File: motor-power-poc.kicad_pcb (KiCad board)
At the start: 4 copper layers, 70 x 50 mm, 160 parts, among them J1 Conn_01x04_Pin, J2 USB_C_Receptacle_USB2.0_14P, J3 Conn_01x02, J4 Conn_02x02_Counter_Clockwise, J5 Conn_02x06_Counter_Clockwise, M1 Motor_Servo, M2 Motor_Servo, M3 DC, Q1 Q_NMOS, Q10 Q_NMOS, Q2 Q_NMOS, Q3 Q_NMOS, Q4 Q_NMOS, Q5 Q_NMOS, Q6 Q_NMOS, Q7 Q_NMOS, Q8 Q_NMOS, Q9 Q_NMOS, SW1 SW_Push, SW2 SW_Push, U1 QRE1113GR, U10 CJ431, U11 DRV8701, U2 QRE1113GR, U3 QRE1113GR, U4 ESP32-S3FH4R2, U5 LM74502, U6 TPS5430DDA, U7 TPS56A37, U8 TPS2121, U9 LDL212PV33R, Y1 48M

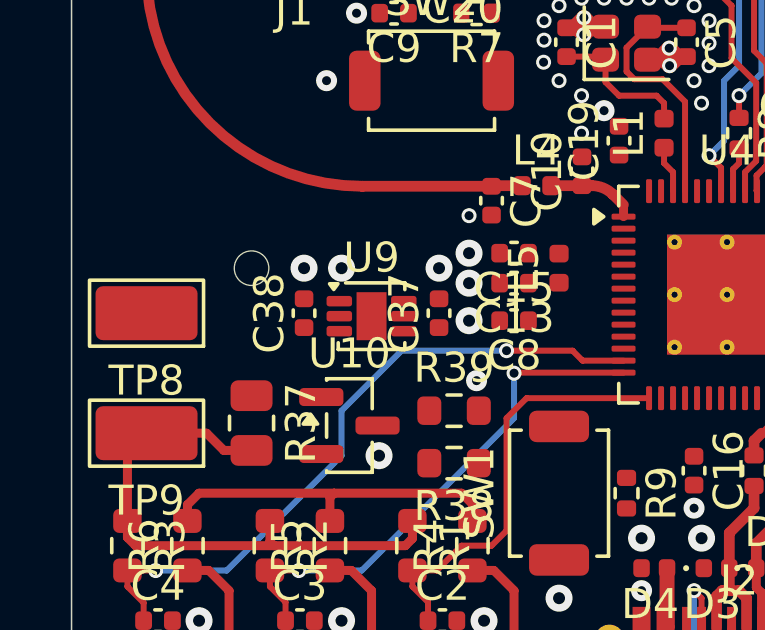
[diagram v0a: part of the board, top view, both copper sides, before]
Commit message: pcb: add 3v3 ldo routing
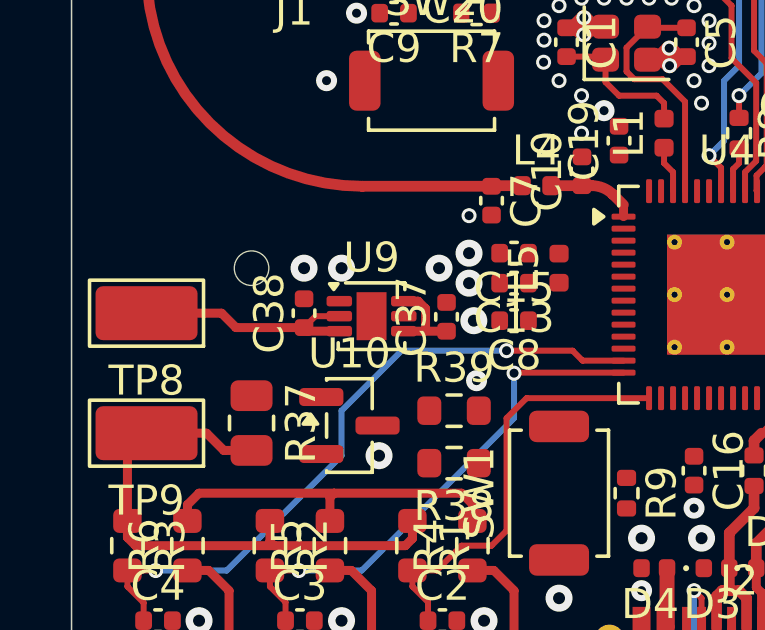
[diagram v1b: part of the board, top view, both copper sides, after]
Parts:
- moved C37 0.28 mm to (124.5, 85.6)
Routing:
- net +3V3: track 11.9 -> 19.9 mm
- net +5V: track 0.00 -> 2.75 mm
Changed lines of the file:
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@@
 	(footprint "Capacitor_SMD:C_0402_1005Metric"
 		(layer "F.Cu")
-		(at 124.25 85.5 90)
+		(at 124.5 85.62143 90)
 		(descr "Capacitor SMD 0402 (1005 Metric), square (rectangular) end terminal, IPC-7351 nominal, (Body size source: IPC-SM-782 page 76, https://www.pcb-3d.com/wordpress/wp-content/uploads/ipc-sm-782a_amendment_1_and_2.pdf), generated with kicad-footprint-generator")
 		(tags "capacitor")
@@
 	)
 	(segment
+		(start 120.925 86.1)
+		(end 119.87 86.1)
+		(width 0.3)
+		(layer "F.Cu")
+		(net 9)
+	)
+	(segment
+		(start 119.87 86.1)
+		(end 119.75 85.98)
+		(width 0.3)
+		(layer "F.Cu")
+		(net 9)
+	)
+	(segment
+		(start 120.925 85.6)
+		(end 120.13 85.6)
+		(width 0.2)
+		(layer "F.Cu")
+		(net 9)
+	)
+	(segment
 		(start 125.3625 91.8625)
 		(end 125.3625 92.425)
@@
 	)
 	(segment
+		(start 119.75 85.98)
+		(end 117.48 85.98)
+		(width 0.3)
+		(layer "F.Cu")
+		(net 9)
+	)
+	(segment
 		(start 120.6125 92.425)
 		(end 120.6125 91.6375)
@@
 	)
 	(segment
+		(start 120.13 85.6)
+		(end 119.75 85.98)
+		(width 0.2)
+		(layer "F.Cu")
+		(net 9)
+	)
+	(segment
+		(start 117.48 85.98)
+		(end 117 85.5)
+		(width 0.3)
+		(layer "F.Cu")
+		(net 9)
+	)
+	(segment
+		(start 117 85.5)
+		(end 114.5 85.5)
+		(width 0.3)
+		(layer "F.Cu")
+		(net 9)
+	)
+	(segment
 		(start 115.8625 92.425)
 		(end 115.8625 91.8875)
@@
 	)
 	(segment
+		(start 124.220766 86.10143)
+		(end 123.75 86.10143)
+		(width 0.3)
+		(layer "F.Cu")
+		(net 14)
+	)
+	(segment
+		(start 123.551848 85.1)
+		(end 123.075 85.1)
+		(width 0.3)
+		(layer "F.Cu")
+		(net 14)
+	)
+	(segment
+		(start 123.801 86.05043)
+		(end 123.801 85.349152)
+		(width 0.3)
+		(layer "F.Cu")
+		(net 14)
+	)
+	(segment
+		(start 123.801 85.349152)
+		(end 123.551848 85.1)
+		(width 0.3)
+		(layer "F.Cu")
+		(net 14)
+	)
+	(segment
+		(start 123.75 86.10143)
+		(end 123.801 86.05043)
+		(width 0.3)
+		(layer "F.Cu")
+		(net 14)
+	)
+	(segment
+		(start 123.75 86.10143)
+		(end 123.07643 86.10143)
+		(width 0.3)
+		(layer "F.Cu")
+		(net 14)
+	)
+	(segment
+		(start 123.07643 86.10143)
+		(end 123.075 86.1)
+		(width 0.3)
+		(layer "F.Cu")
+		(net 14)
+	)
+	(segment
 		(start 168.9 87.6)
 		(end 169 87.5)
@@
 	)
 	(via
-		(at 125.25 85.75)
+		(at 125.409159 85.750326)
 		(size 0.9)
 		(drill 0.4)

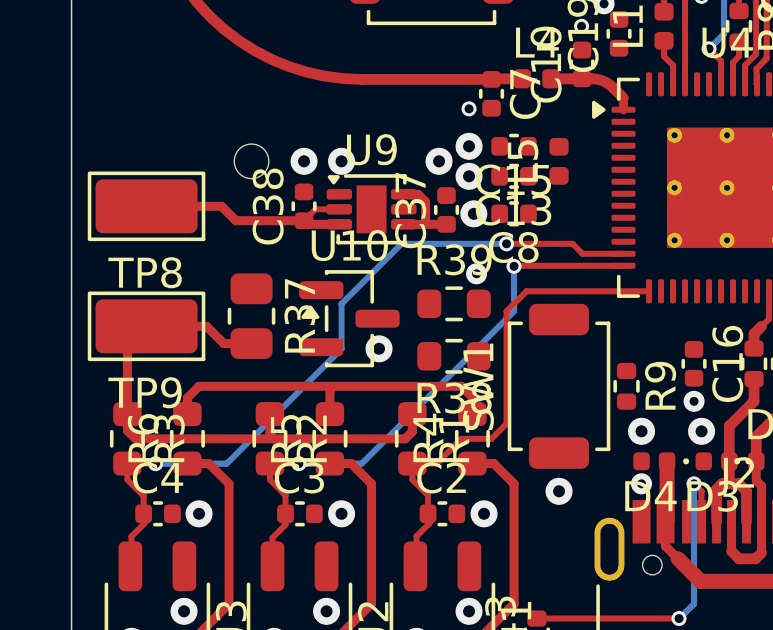
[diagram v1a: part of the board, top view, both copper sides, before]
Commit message: pcb: add 3v reference routing
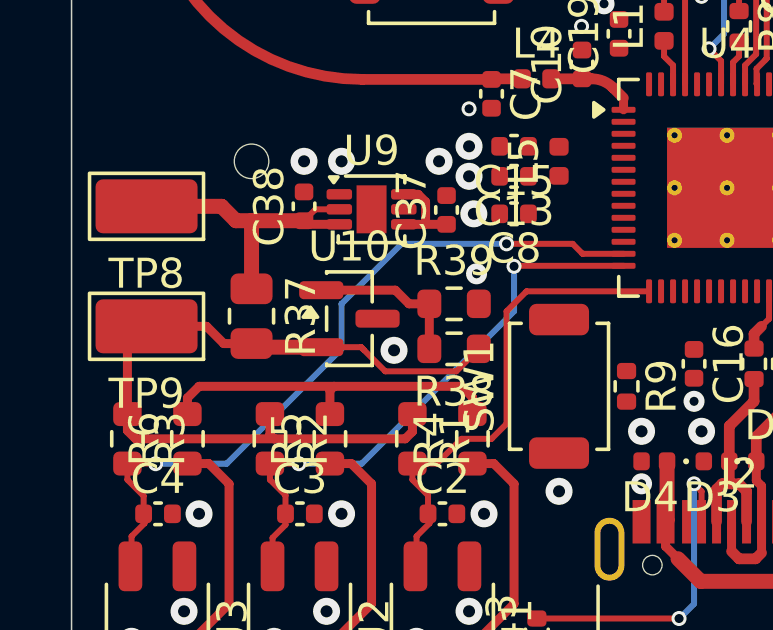
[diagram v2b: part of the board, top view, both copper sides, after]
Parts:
- moved R38 0.25 mm to (124.8, 90.2)
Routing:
- net +3V: track 18.7 -> 27.0 mm
- net Net-(U10-REF): track 0.00 -> 5.54 mm
- net +3V3: track 19.9 -> 22.2 mm
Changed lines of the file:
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@@
 	(footprint "Resistor_SMD:R_0603_1608Metric"
 		(layer "F.Cu")
-		(at 124.75 90.5 180)
+		(at 124.75 90.25 180)
 		(descr "Resistor SMD 0603 (1608 Metric), square (rectangular) end terminal, IPC-7351 nominal, (Body size source: IPC-SM-782 page 72, https://www.pcb-3d.com/wordpress/wp-content/uploads/ipc-sm-782a_amendment_1_and_2.pdf), generated with kicad-footprint-generator")
 		(tags "resistor")
@@
 	)
 	(segment
+		(start 119.75 85.98)
+		(end 118 85.98)
+		(width 0.5)
+		(layer "F.Cu")
+		(net 9)
+	)
+	(segment
 		(start 120.925 85.6)
 		(end 120.13 85.6)
@@
 	)
 	(segment
-		(start 119.75 85.98)
+		(start 118 85.98)
 		(end 117.48 85.98)
-		(width 0.3)
+		(width 0.5)
 		(layer "F.Cu")
 		(net 9)
@@
 	)
 	(segment
+		(start 118 88.25)
+		(end 118 85.98)
+		(width 0.5)
+		(layer "F.Cu")
+		(net 9)
+	)
+	(segment
 		(start 120.13 85.6)
 		(end 119.75 85.98)
@@
 		(start 117.48 85.98)
 		(end 117 85.5)
-		(width 0.3)
+		(width 0.5)
 		(layer "F.Cu")
 		(net 9)
@@
 		(start 117 85.5)
 		(end 114.5 85.5)
-		(width 0.3)
+		(width 0.5)
 		(layer "F.Cu")
 		(net 9)
@@
 	)
 	(segment
+		(start 121.729318 90.270682)
+		(end 121.653179 90.194543)
+		(width 0.2)
+		(layer "F.Cu")
+		(net 54)
+	)
+	(segment
+		(start 121.653636 90.195)
+		(end 120.325 90.195)
+		(width 0.2)
+		(layer "F.Cu")
+		(net 54)
+	)
+	(segment
 		(start 114.1375 93.25)
 		(end 113.8625 92.975)
@@
 	)
 	(segment
+		(start 124.825 91)
+		(end 122.458636 91)
+		(width 0.2)
+		(layer "F.Cu")
+		(net 54)
+	)
+	(segment
 		(start 123.124 93.25)
 		(end 118.75 93.25)
@@
 	)
 	(segment
+		(start 122.458636 91)
+		(end 121.729318 90.270682)
+		(width 0.2)
+		(layer "F.Cu")
+		(net 54)
+	)
+	(segment
 		(start 113.8625 92.425)
 		(end 113.8625 90.1375)
@@
 	)
 	(segment
+		(start 120.325 90.195)
+		(end 118.12 90.195)
+		(width 0.5)
+		(layer "F.Cu")
+		(net 54)
+	)
+	(segment
+		(start 121.729318 90.270682)
+		(end 121.653636 90.195)
+		(width 0.2)
+		(layer "F.Cu")
+		(net 54)
+	)
+	(segment
 		(start 123.3625 92.425)
 		(end 123.3625 93.0115)
@@
 	)
 	(segment
+		(start 118.12 90.195)
+		(end 118 90.075)
+		(width 0.5)
+		(layer "F.Cu")
+		(net 54)
+	)
+	(segment
 		(start 123.3625 93.0115)
 		(end 123.124 93.25)
@@
 	)
 	(segment
+		(start 125.575 90.25)
+		(end 124.825 91)
+		(width 0.2)
+		(layer "F.Cu")
+		(net 54)
+	)
+	(segment
 		(start 118.6125 93.1125)
 		(end 118.75 93.25)
@@
 	)
 	(segment
+		(start 123.925 90.5)
+		(end 123.925 88.75)
+		(width 0.3)
+		(layer "F.Cu")
+		(net 70)
+	)
+	(segment
+		(start 123.925 88.75)
+		(end 123.25 88.75)
+		(width 0.3)
+		(layer "F.Cu")
+		(net 70)
+	)
+	(segment
+		(start 122.795 88.295)
+		(end 120.325 88.295)
+		(width 0.3)
+		(layer "F.Cu")
+		(net 70)
+	)
+	(segment
+		(start 123.25 88.75)
+		(end 122.795 88.295)
+		(width 0.3)
+		(layer "F.Cu")
+		(net 70)
+	)
+	(segment
 		(start 179 87.1445)
 		(end 179 85.25)
@@
 	)
 	(via
-		(at 122.25 90.25)
+		(at 122.75 90.3)
 		(size 0.9)
 		(drill 0.4)

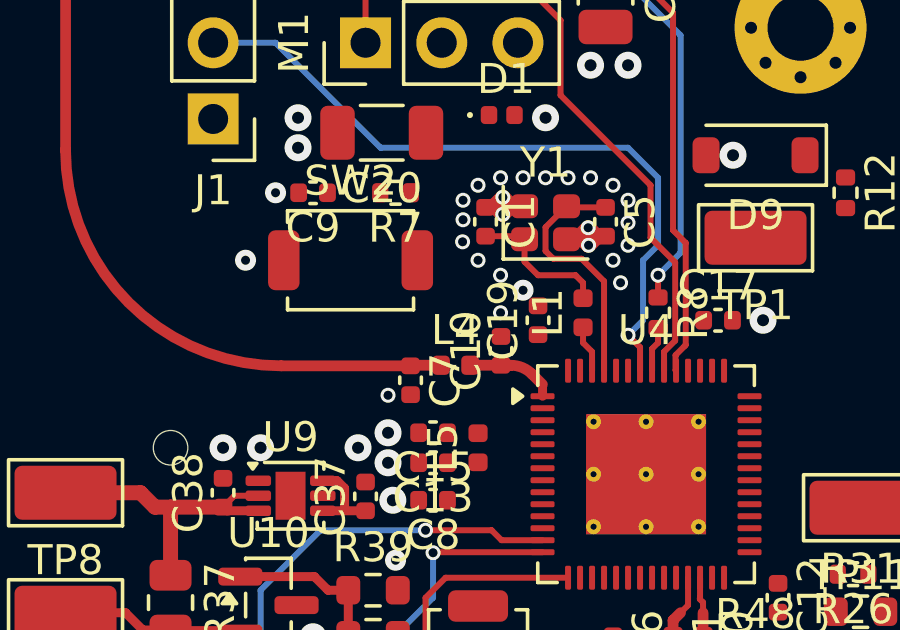
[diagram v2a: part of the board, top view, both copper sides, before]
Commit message: pcb: add CHIP_PU routing
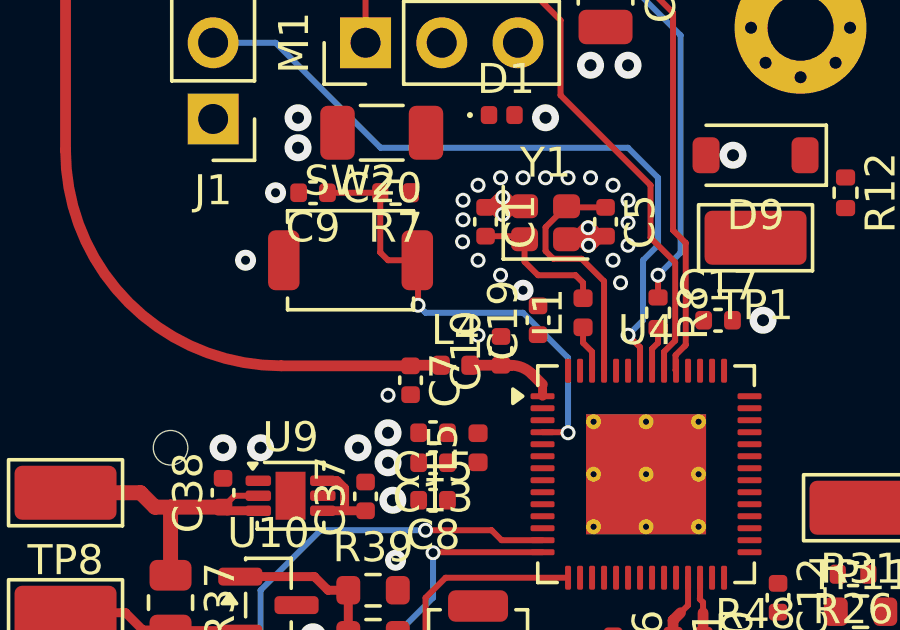
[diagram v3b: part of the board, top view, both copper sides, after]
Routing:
- net /CHIP_PU: track 0.00 -> 15.7 mm, vias 0 -> 2
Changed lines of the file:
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@@
+	)
+	(segment
+		(start 126.225 77.75)
+		(end 125.25 77.75)
+		(width 0.2)
+		(layer "F.Cu")
+		(net 10)
+	)
+	(segment
+		(start 131.2325 83.4825)
+		(end 131.25 83.5)
+		(width 0.2)
+		(layer "F.Cu")
+		(net 10)
+	)
+	(segment
+		(start 125.25 77.75)
+		(end 124.99 77.49)
+		(width 0.2)
+		(layer "F.Cu")
+		(net 10)
+	)
+	(segment
+		(start 126.25 79.25)
+		(end 126.25 77.775)
+		(width 0.2)
+		(layer "F.Cu")
+		(net 10)
+	)
+	(segment
+		(start 123.23 75.5)
+		(end 124.99 75.5)
+		(width 0.2)
+		(layer "F.Cu")
+		(net 10)
+	)
+	(segment
+		(start 126.25 77.775)
+		(end 126.225 77.75)
+		(width 0.2)
+		(layer "F.Cu")
+		(net 10)
+	)
+	(segment
+		(start 130.4 83.4825)
+		(end 131.2325 83.4825)
+		(width 0.2)
+		(layer "F.Cu")
+		(net 10)
+	)
+	(segment
+		(start 124.99 77.49)
+		(end 124.99 75.5)
+		(width 0.2)
+		(layer "F.Cu")
+		(net 10)
+	)
+	(via
+		(at 126.25 79.25)
+		(size 0.5)
+		(drill 0.3)
+		(layers "F.Cu" "B.Cu")
+		(net 10)
+	)
+	(via
+		(at 131.25 83.5)
+		(size 0.5)
+		(drill 0.3)
+		(layers "F.Cu" "B.Cu")
+		(net 10)
+	)
+	(segment
+		(start 129.75 79.5)
+		(end 126.5 79.5)
+		(width 0.2)
+		(layer "B.Cu")
+		(net 10)
+	)
+	(segment
+		(start 126.5 79.5)
+		(end 126.25 79.25)
+		(width 0.2)
+		(layer "B.Cu")
+		(net 10)
+	)
+	(segment
+		(start 131.25 83.5)
+		(end 131.25 81)
+		(width 0.2)
+		(layer "B.Cu")
+		(net 10)
+	)
+	(segment
+		(start 131.25 81)
+		(end 129.75 79.5)
+		(width 0.2)
+		(layer "B.Cu")
+		(net 10)
 	)
 	(segment
@@
 	)
 	(via
-		(at 129 79.5)
-		(size 0.5)
-		(drill 0.3)
+		(at 128.25 80.25)
+		(size 0.5)
+		(drill 0.3)

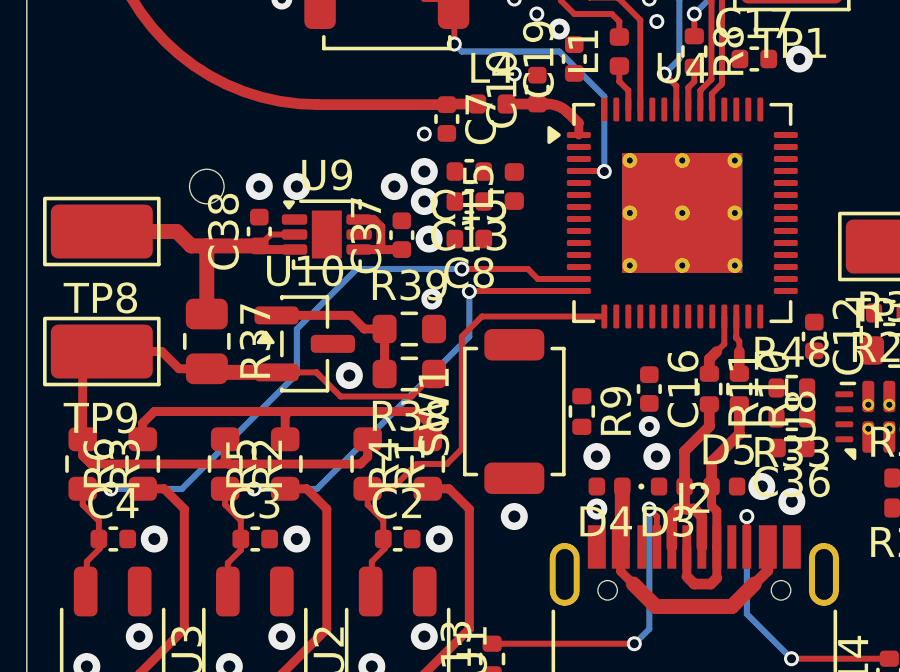
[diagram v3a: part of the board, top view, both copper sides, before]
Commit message: pcb: add BOOT routing
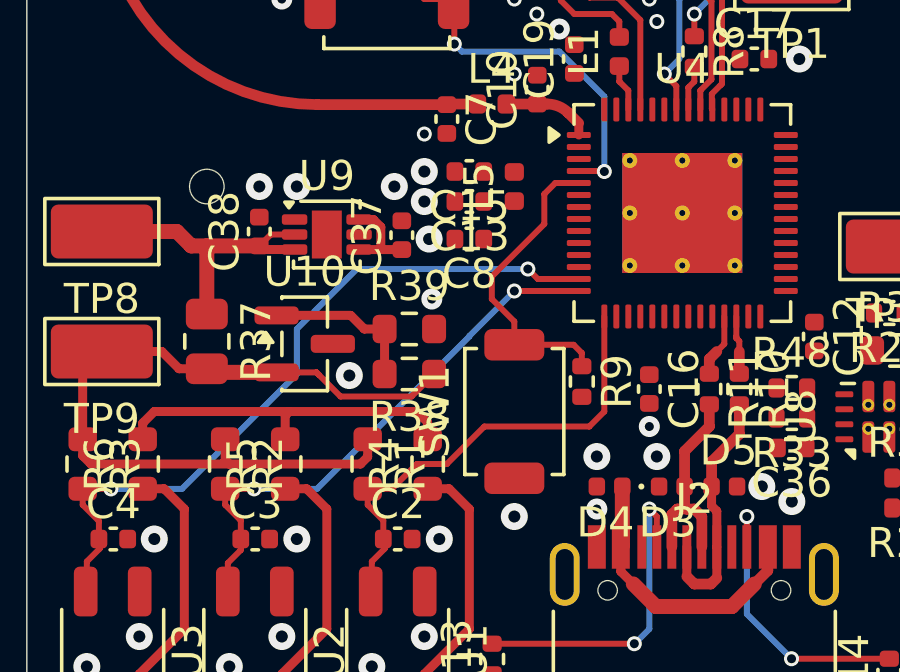
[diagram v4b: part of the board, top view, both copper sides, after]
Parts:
- moved R9 1.00 mm to (130.5, 90.5)
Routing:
- net /BOOT: track 0.00 -> 10.2 mm
- net /LS2: track 19.2 -> 18.4 mm
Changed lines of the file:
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@@
 	(footprint "Resistor_SMD:R_0402_1005Metric"
 		(layer "F.Cu")
-		(at 130.5 91.5 -90)
+		(at 130.5 90.5 -90)
 		(descr "Resistor SMD 0402 (1005 Metric), square (rectangular) end terminal, IPC-7351 nominal, (Body size source: IPC-SM-782 page 72, https://www.pcb-3d.com/wordpress/wp-content/uploads/ipc-sm-782a_amendment_1_and_2.pdf), generated with kicad-footprint-generator")
 		(tags "resistor")
@@
 	)
 	(segment
+		(start 127.25 92)
+		(end 130.75 92)
+		(width 0.2)
+		(layer "F.Cu")
+		(net 3)
+	)
+	(segment
 		(start 123.8825 95.1325)
 		(end 123.3625 94.6125)
@@
 	)
 	(segment
-		(start 127.1675 88.3325)
-		(end 131.25 88.3325)
+		(start 125 93.25)
+		(end 126 93.25)
 		(width 0.2)
 		(layer "F.Cu")
@@
 	)
 	(segment
-		(start 126.5 92.75)
-		(end 126.5 89)
+		(start 130.75 92)
+		(end 131.25 91.5)
 		(width 0.2)
 		(layer "F.Cu")
@@
 	)
 	(segment
-		(start 123.3625 94.075)
-		(end 124.175 94.075)
+		(start 131.25 91.5)
+		(end 131.25 88.3325)
 		(width 0.2)
 		(layer "F.Cu")
@@
 	)
 	(segment
-		(start 125 93.25)
-		(end 126 93.25)
+		(start 126 93.25)
+		(end 127.25 92)
+		(width 0.2)
+		(layer "F.Cu")
+		(net 3)
+	)
+	(segment
+		(start 123.3625 94.075)
+		(end 124.175 94.075)
 		(width 0.2)
 		(layer "F.Cu")
@@
 	)
 	(segment
-		(start 126.5 89)
-		(end 127.1675 88.3325)
-		(width 0.2)
-		(layer "F.Cu")
-		(net 3)
-	)
-	(segment
-		(start 126 93.25)
-		(end 126.5 92.75)
-		(width 0.2)
-		(layer "F.Cu")
-		(net 3)
-	)
-	(segment
 		(start 118.7 96.55)
 		(end 119.1325 96.1175)
@@
 	)
 	(segment
-		(start 126.7675 87.4825)
-		(end 126.75 87.5)
-		(width 0.2)
-		(layer "F.Cu")
-		(net 4)
-	)
-	(segment
 		(start 119.1325 95.1325)
 		(end 118.6125 94.6125)
@@
 	)
 	(segment
-		(start 130.4 87.4825)
-		(end 126.7675 87.4825)
+		(start 128.25 87.4825)
+		(end 130.4 87.4825)
 		(width 0.2)
 		(layer "F.Cu")
@@
 	)
 	(via
-		(at 126.75 87.5)
+		(at 128.25 87.4825)
 		(size 0.5)
 		(drill 0.3)
@@
 	)
 	(segment
-		(start 119.576653 94.07944)
+		(start 126.75 89)
 		(end 121.67056 94.07944)
 		(width 0.2)
@@
 	)
 	(segment
-		(start 126.75 89)
-		(end 126.75 87.5)
+		(start 126.75 88.9825)
+		(end 126.75 89)
 		(width 0.2)
 		(layer "B.Cu")
@@
 	(segment
 		(start 121.67056 94.07944)
-		(end 126.75 89)
+		(end 119.576653 94.07944)
+		(width 0.2)
+		(layer "B.Cu")
+		(net 4)
+	)
+	(segment
+		(start 128.25 87.4825)
+		(end 126.75 88.9825)
 		(width 0.2)
 		(layer "B.Cu")
@@
 	)
 	(segment
+		(start 129.034166 87.0825)
+		(end 130.4 87.0825)
+		(width 0.2)
+		(layer "F.Cu")
+		(net 5)
+	)
+	(segment
 		(start 114 97.45)
 		(end 114 96.5)
@@
 	)
 	(segment
-		(start 129.034166 87.0825)
-		(end 130.4 87.0825)
-		(width 0.2)
-		(layer "F.Cu")
-		(net 5)
-	)
-	(segment
-		(start 126.5 86.75)
-		(end 128.701666 86.75)
-		(width 0.2)
-		(layer "F.Cu")
-		(net 5)
-	)
-	(segment
 		(start 114.4325 96.0675)
 		(end 114.4325 95.7)
@@
 	)
 	(via
-		(at 126.5 86.75)
+		(at 128.701666 86.75)
 		(size 0.5)
 		(drill 0.3)
@@
 	)
 	(segment
-		(start 117.17056 94.07944)
-		(end 114.803296 94.07944)
+		(start 128.701666 86.75)
+		(end 123 86.75)
 		(width 0.2)
 		(layer "B.Cu")
@@
 	)
 	(segment
-		(start 126.5 86.75)
-		(end 123 86.75)
+		(start 123 86.75)
+		(end 121 88.75)
 		(width 0.2)
 		(layer "B.Cu")
@@
 	)
 	(segment
-		(start 123 86.75)
-		(end 121 88.75)
+		(start 117.17056 94.07944)
+		(end 114.803296 94.07944)
 		(width 0.2)
 		(layer "B.Cu")
@@
 	)
 	(segment
+		(start 130.5 89.55)
+		(end 130.225 89.275)
+		(width 0.2)
+		(layer "F.Cu")
+		(net 59)
+	)
+	(segment
+		(start 129.25 84.25)
+		(end 129.6175 83.8825)
+		(width 0.2)
+		(layer "F.Cu")
+		(net 59)
+	)
+	(segment
+		(start 129.25 85.25)
+		(end 129.25 84.25)
+		(width 0.2)
+		(layer "F.Cu")
+		(net 59)
+	)
+	(segment
+		(start 130.5 89.99)
+		(end 130.5 89.55)
+		(width 0.2)
+		(layer "F.Cu")
+		(net 59)
+	)
+	(segment
+		(start 128.25 89.275)
+		(end 128.25 88.5)
+		(width 0.2)
+		(layer "F.Cu")
+		(net 59)
+	)
+	(segment
+		(start 127.5 87.75)
+		(end 127.5 87)
+		(width 0.2)
+		(layer "F.Cu")
+		(net 59)
+	)
+	(segment
+		(start 127.5 87)
+		(end 129.25 85.25)
+		(width 0.2)
+		(layer "F.Cu")
+		(net 59)
+	)
+	(segment
+		(start 128.25 88.5)
+		(end 127.5 87.75)
+		(width 0.2)
+		(layer "F.Cu")
+		(net 59)
+	)
+	(segment
+		(start 130.225 89.275)
+		(end 128.25 89.275)
+		(width 0.2)
+		(layer "F.Cu")
+		(net 59)
+	)
+	(segment
+		(start 129.6175 83.8825)
+		(end 130.4 83.8825)
+		(width 0.2)
+		(layer "F.Cu")
+		(net 59)
+	)
+	(segment

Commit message: pcb: add TPS2121 power mux routing
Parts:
- moved R27 0.11 mm to (141.2, 94.7)
- moved R32 0.11 mm to (141.2, 93.7)
- moved R26 0.06 mm to (140.7, 88.2)
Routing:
- net Net-(U8-OV1): track 0.00 -> 6.54 mm
- net Net-(U8-OV2): track 0.00 -> 6.30 mm
- net Net-(U8-CP2): track 0.00 -> 3.57 mm
- net +5V_buck: track 0.00 -> 3.30 mm
- net Net-(U8-PR1): track 0.00 -> 2.83 mm
- net +Vbus: track 9.52 -> 11.9 mm
- net Net-(U8-SS): track 0.00 -> 1.83 mm
- net Net-(U8-ILM): track 0.00 -> 1.36 mm
- net ST: track 0.00 -> 1.33 mm
- net /LS3: track 24.4 -> 23.5 mm
- net GND: vias 116 -> 117

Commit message: pcb: set thermal vias connections to solid
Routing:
- net GND: vias 117 -> 118
